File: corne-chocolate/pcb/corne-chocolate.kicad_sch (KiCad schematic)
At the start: 87 parts, among them J1 MJ-4PP-9, J2 OLED, J3 LED, P1 i2c-pin, P2 i2c-pin, SW1 SW_PUSH, SW10 SW_PUSH, SW11 SW_PUSH, SW12 SW_PUSH, SW13 SW_PUSH, SW14 SW_PUSH, SW15 SW_PUSH, SW16 SW_PUSH, SW17 SW_PUSH, SW18 SW_PUSH, SW19 SW_PUSH, SW2 SW_PUSH, SW20 SW_PUSH, SW21 SW_PUSH, SW3 SW_PUSH, SW4 SW_PUSH, SW5 SW_PUSH, SW6 SW_PUSH, SW7 SW_PUSH, SW8 SW_PUSH, SW9 SW_PUSH, U1 ProMicro

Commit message: Cleanup schematic
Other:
- note added: "Key Matrix"
- note added: "LEDs"
- note added: "per-key"
- note added: "underglow"
- moved on the sheet: D1, D10, D11, D12, D13, D14, D15, D16, D17, D18, D19, D2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

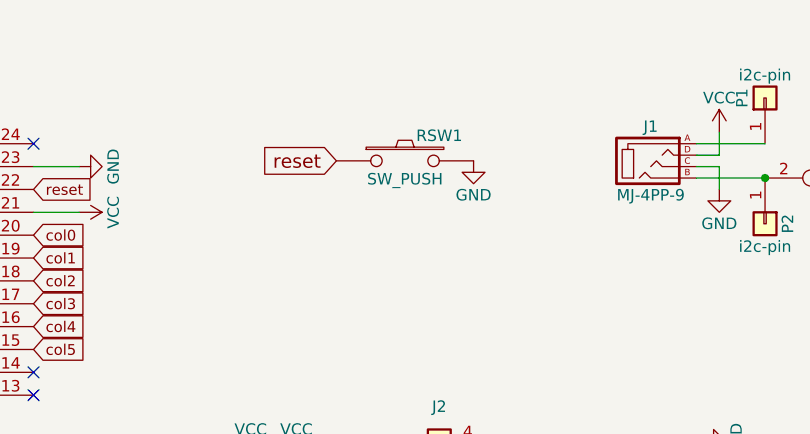
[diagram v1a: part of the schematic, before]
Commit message: cleanup symbol library. copy symbols from pcb to new project specific library
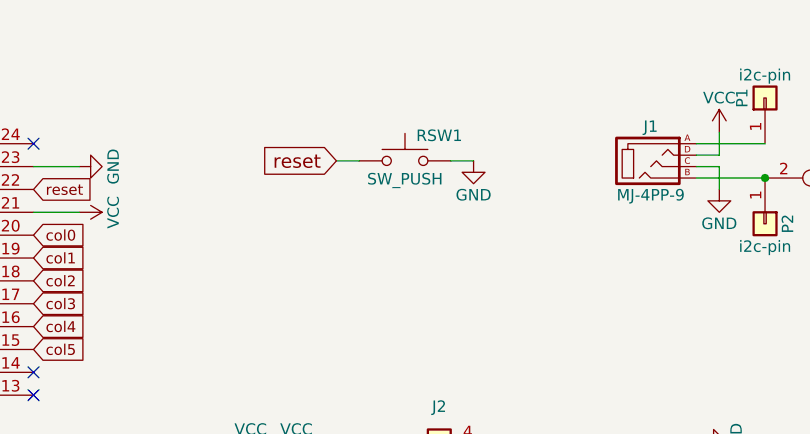
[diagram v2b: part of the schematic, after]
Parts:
- D1, D10, D11, D12, D13, D14, D15, D16, D17, D18, D19, D2, D20, D21, D3, D4, D5, D6, D7, D8, D9: footprint kbd:D3_TH_SMD -> corne-chocolate:D3_SMD
- J1: symbol corne-chocolate-rescue:MJ-4PP-9-kbd -> kbd:MJ-4PP-9
- L22, L23, L24, L25, L26, L27: footprint kbd:SK6812MINI_underglow -> kbd:SK6812MINI_underglow_rev
- RSW1: symbol corne-chocolate-rescue:SW_PUSH-kbd -> Switch:SW_Push
- SW1, SW10, SW11, SW12, SW13, SW14, SW15, SW16, SW17, SW18, SW19, SW2, SW20, SW3, SW4, SW5, SW6, SW7, SW8, SW9: footprint kbd:MX_ALPS_PG1350_noLed -> corne-chocolate:Choc_Hotswap
- SW21: footprint kbd:MX_ALPS_PG1350_noLed_1.75u -> corne-chocolate:Choc_Hotswap_1.5u

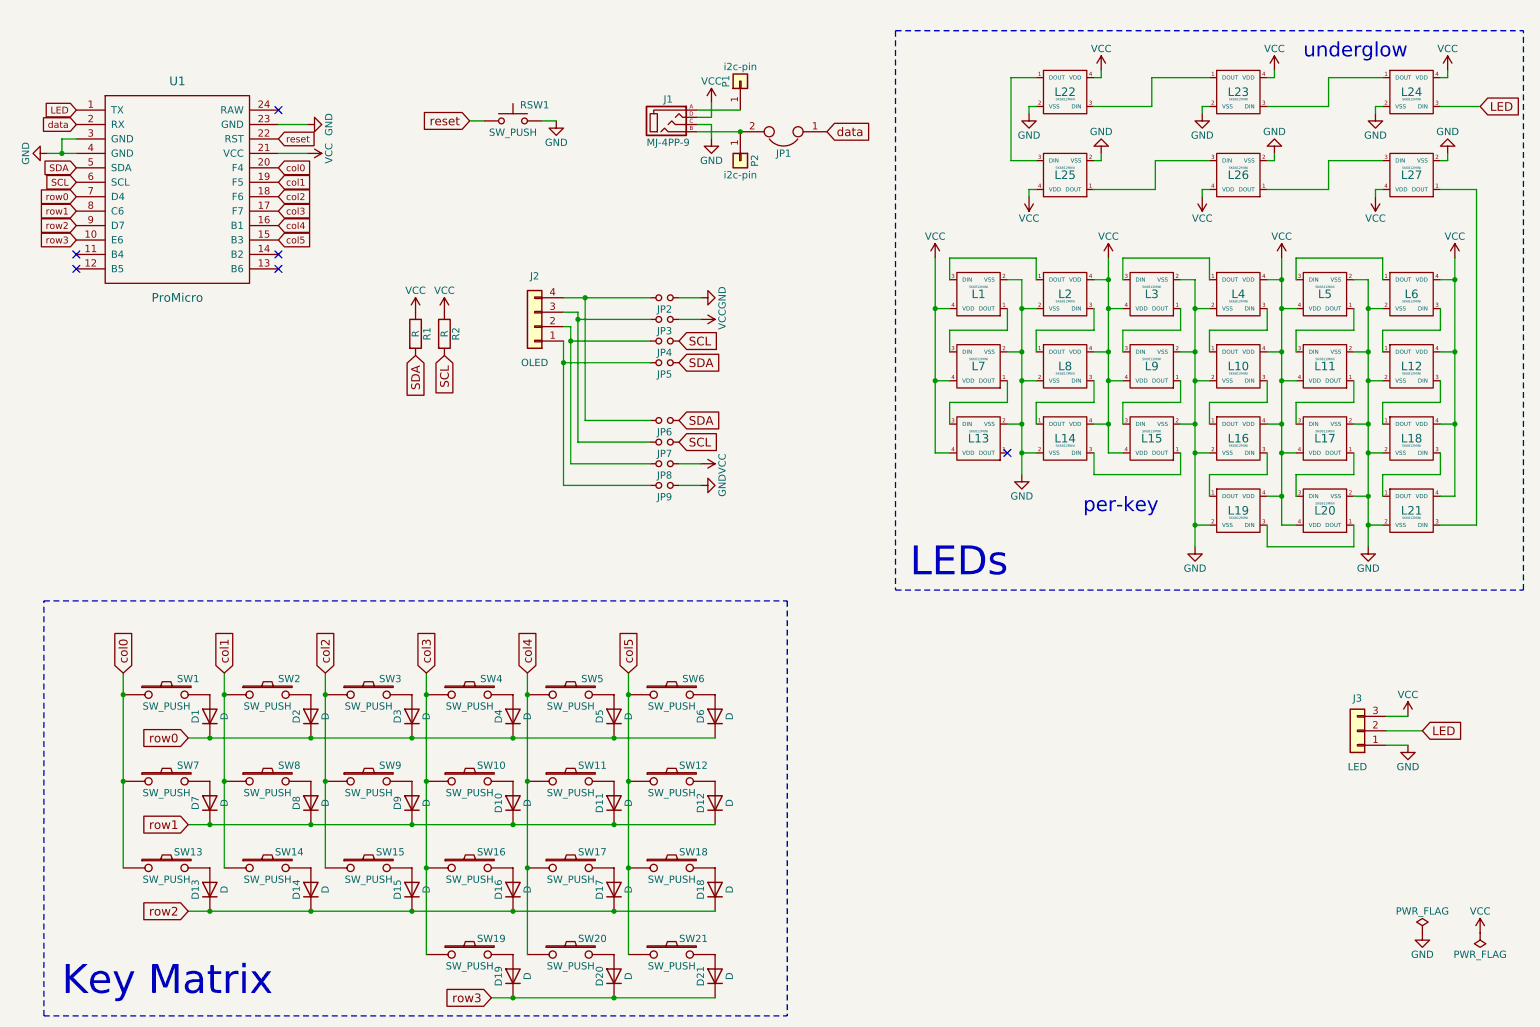
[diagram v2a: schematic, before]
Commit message: corne-chocolate first modified version by timlauber: first cleanup of schematic and layout
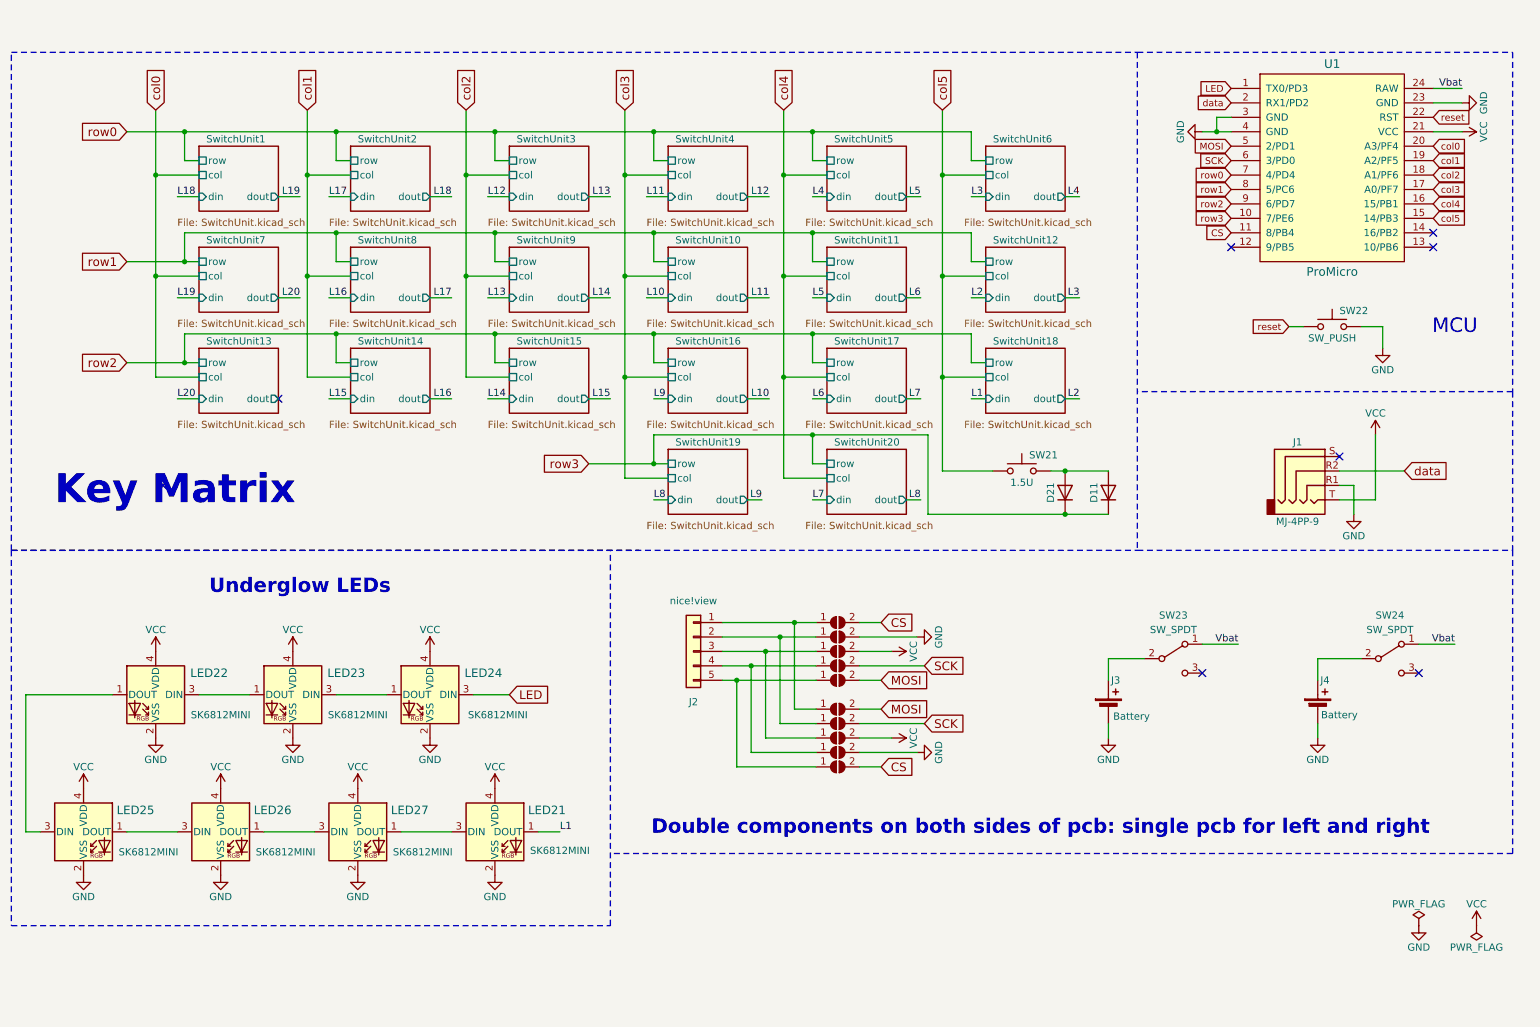
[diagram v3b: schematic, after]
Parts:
- removed D1, D10, D12, D13, D14, D15, D16, D17, D18, D19, D2, D20, D3, D4, D5, D6, D7, D8, D9: D, corne-chocolate:D3_SMD, symbol Device:D
- removed J3: LED, kbd:StripLED_rev, symbol Connector_Generic:Conn_01x03
- removed JP1: (no value), kbd:JPC2, symbol corne-chocolate-rescue:Jumper-Device
- removed JP2, JP3, JP4, JP5, JP6, JP7, JP8, JP9: (no value), kbd:Jumper, symbol corne-chocolate-rescue:Jumper_NO_Small-Device
- removed L1, L10, L11, L12, L13, L14, L15, L16, L17, L18, L19, L2, L20, L3, L4, L5, L6, L7, L8, L9: SK6812MINI, kbd:SK6812MINI_rev, symbol corne-chocolate-rescue:SK6812MINI-kbd
- removed P1, P2: i2c-pin, kbd:1pin_conn, symbol Connector_Generic:Conn_01x01
- removed R1, R2: R, kbd:R, symbol Device:R
- removed RSW1: SW_PUSH, kbd:ResetSW, symbol Switch:SW_Push
- removed SW1, SW10, SW11, SW12, SW13, SW14, SW15, SW16, SW17, SW18, SW19, SW2, SW20, SW3, SW4, SW5, SW6, SW7, SW8, SW9: SW_PUSH, corne-chocolate:Choc_Hotswap, symbol corne-chocolate-rescue:SW_PUSH-kbd
- added J3, J4: Battery, Connector_JST:JST_PH_S2B-PH-SM4-TB_1x02-1MP_P2.00mm_Horizontal, symbol Device:Battery_Cell
- added JP10, JP11, JP2, JP3, JP4, JP5, JP6, JP7, JP8, JP9: SolderJumper_2_Open, Resistor_SMD:R_0603_1608Metric, symbol Jumper:SolderJumper_2_Open
- added SW22: SW_PUSH, corne-chocolate:ResetSW, symbol Switch:SW_Push
- added SW23, SW24: SW_SPDT, Button_Switch_SMD:SW_SPDT_PCM12, symbol Switch:SW_SPDT
- D11, D21: value D -> 1N4148; footprint corne-chocolate:D3_SMD -> Diode_SMD:D_SOD-323_HandSoldering
- J1: footprint kbd:MJ-4PP-9 -> corne-chocolate:MJ-4PP-9; symbol kbd:MJ-4PP-9 -> Connector_Audio:AudioJack4
- J2: value OLED -> nice!view; footprint kbd:OLED -> Connector_PinHeader_2.54mm:PinHeader_1x05_P2.54mm_Vertical; symbol Connector_Generic:Conn_01x04 -> Connector_Generic:Conn_01x05
- LED21: renamed from L21; footprint kbd:SK6812MINI_rev -> LED_SMD:LED_SK6812MINI_PLCC4_3.5x3.5mm_P1.75mm; symbol corne-chocolate-rescue:SK6812MINI-kbd -> LED:SK6812MINI
- LED22: renamed from L22; footprint kbd:SK6812MINI_underglow_rev -> LED_SMD:LED_SK6812MINI_PLCC4_3.5x3.5mm_P1.75mm; symbol corne-chocolate-rescue:SK6812MINI-kbd -> LED:SK6812MINI
- LED23: renamed from L23; footprint kbd:SK6812MINI_underglow_rev -> LED_SMD:LED_SK6812MINI_PLCC4_3.5x3.5mm_P1.75mm; symbol corne-chocolate-rescue:SK6812MINI-kbd -> LED:SK6812MINI
- LED24: renamed from L24; footprint kbd:SK6812MINI_underglow_rev -> LED_SMD:LED_SK6812MINI_PLCC4_3.5x3.5mm_P1.75mm; symbol corne-chocolate-rescue:SK6812MINI-kbd -> LED:SK6812MINI
- LED25: renamed from L25; footprint kbd:SK6812MINI_underglow_rev -> LED_SMD:LED_SK6812MINI_PLCC4_3.5x3.5mm_P1.75mm; symbol corne-chocolate-rescue:SK6812MINI-kbd -> LED:SK6812MINI
- LED26: renamed from L26; footprint kbd:SK6812MINI_underglow_rev -> LED_SMD:LED_SK6812MINI_PLCC4_3.5x3.5mm_P1.75mm; symbol corne-chocolate-rescue:SK6812MINI-kbd -> LED:SK6812MINI
- LED27: renamed from L27; footprint kbd:SK6812MINI_underglow_rev -> LED_SMD:LED_SK6812MINI_PLCC4_3.5x3.5mm_P1.75mm; symbol corne-chocolate-rescue:SK6812MINI-kbd -> LED:SK6812MINI
- SW21: value SW_PUSH -> 1.5U; symbol corne-chocolate-rescue:SW_PUSH-kbd -> Switch:SW_Push
- U1: footprint kbd:ProMicro_v2 -> corne-chocolate:ProMicro_v2; symbol corne-chocolate-rescue:ProMicro-kbd -> corne:ProMicro
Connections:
- net GND: now also J1.R1, J3.2 (-), J4.2 (-), JP10.2 (B), JP3.2 (B), SW22.2; no longer J1.C
- net VCC: now also J1.T, JP4.2 (B), JP9.2 (B); no longer J1.D
- net data: now also J1.R2
- net reset: now also SW22.1
- net row1: no longer D11.1 (K)
- net row3: now also D11.1 (K)
- net CS: now reaches U1.11 (8/PB4)
- net CS: now also JP11.2 (B), JP2.2 (B)
- net Vbat: now reaches U1.24 (RAW)
- net Vbat: now also SW23.1 (A), SW24.1 (A)
- net at D11.2 (A): now also D21.2 (A), SW21.2
- net L1: now reaches LED21.1 (DOUT)
- net at J2.1 (Pin_1): now also JP2.1 (A), JP7.1 (A)
- net at J2.2 (Pin_2): now also JP3.1 (A), JP8.1 (A)
- net at J2.3 (Pin_3): now also JP4.1 (A), JP9.1 (A)
- net at J2.4 (Pin_4): now also JP10.1 (A), JP5.1 (A)
- net SCL renamed SCK
- net SCK: now also JP5.2 (B), JP8.2 (B)
- net SDA renamed MOSI
- net MOSI: now also JP6.2 (B), JP7.2 (B)
- new net: J2.5 (Pin_5), JP11.1 (A), JP6.1 (A)
- new net: J4.1 (+), SW24.2 (B)
- new net: J3.1 (+), SW23.2 (B)
- no-connect marks 6 -> 8
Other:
- added sheet SwitchUnit1 (SwitchUnit.kicad_sch)
- added sheet SwitchUnit10 (SwitchUnit.kicad_sch)
- added sheet SwitchUnit11 (SwitchUnit.kicad_sch)
- added sheet SwitchUnit12 (SwitchUnit.kicad_sch)
- added sheet SwitchUnit13 (SwitchUnit.kicad_sch)
- added sheet SwitchUnit14 (SwitchUnit.kicad_sch)
- added sheet SwitchUnit15 (SwitchUnit.kicad_sch)
- added sheet SwitchUnit16 (SwitchUnit.kicad_sch)
- added sheet SwitchUnit17 (SwitchUnit.kicad_sch)
- added sheet SwitchUnit18 (SwitchUnit.kicad_sch)
- added sheet SwitchUnit19 (SwitchUnit.kicad_sch)
- added sheet SwitchUnit2 (SwitchUnit.kicad_sch)
- added sheet SwitchUnit20 (SwitchUnit.kicad_sch)
- added sheet SwitchUnit3 (SwitchUnit.kicad_sch)
- added sheet SwitchUnit4 (SwitchUnit.kicad_sch)
- added sheet SwitchUnit5 (SwitchUnit.kicad_sch)
- added sheet SwitchUnit6 (SwitchUnit.kicad_sch)
- added sheet SwitchUnit7 (SwitchUnit.kicad_sch)
- added sheet SwitchUnit8 (SwitchUnit.kicad_sch)
- added sheet SwitchUnit9 (SwitchUnit.kicad_sch)
- note added: "Double components on both sides of pcb: single pcb for left and right"
- note added: "MCU"
- note added: "Underglow LEDs"
- note removed: "LEDs"
- note removed: "per-key"
- note removed: "underglow"
- moved on the sheet: D21, SW21
